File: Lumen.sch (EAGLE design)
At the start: 33 parts, among them J1 AVR_SPI_PRG_6PTH, U1 Tiny45-20-SMT, Y1 8Mhz

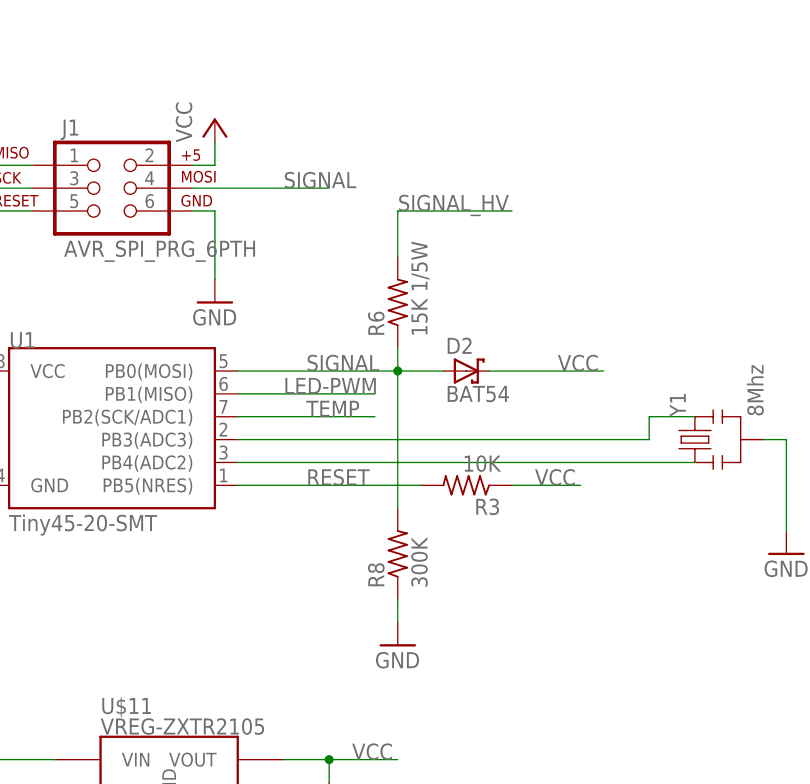
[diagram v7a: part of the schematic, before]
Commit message: Rearranged boards for manufacturability. Changed 0402 footprint.
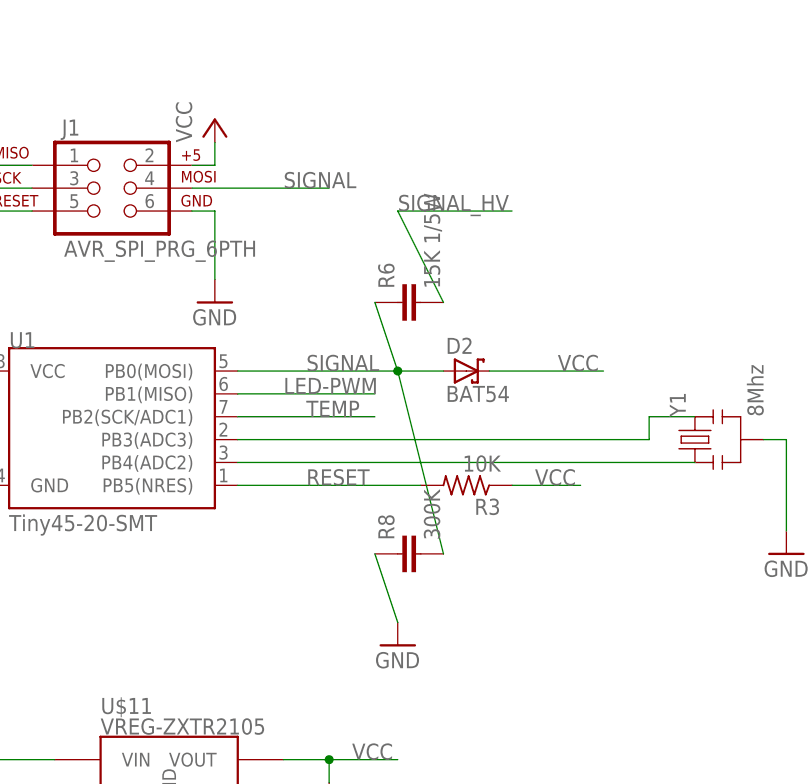
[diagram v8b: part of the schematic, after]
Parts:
- R6, R8: device resistor:R-US_R0402 -> BlueRobotics-Main:C-EUC0402
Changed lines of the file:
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@@
 <part name="R7" library="resistor" deviceset="R-US_" device="R1206" value="NP"/>
 <part name="GND15" library="supply1" deviceset="GND" device=""/>
-<part name="R6" library="resistor" deviceset="R-US_" device="R0402" value="15K 1/5W"/>
-<part name="R8" library="resistor" deviceset="R-US_" device="R0402" value="300K"/>
+<part name="R6" library="BlueRobotics-Main" deviceset="C-EU" device="C0402" value="15K 1/5W"/>
+<part name="R8" library="BlueRobotics-Main" deviceset="C-EU" device="C0402" value="300K"/>
 <part name="Y1" library="SparkFun" deviceset="RESONATOR" device="SMD" value="8Mhz"/>
 </parts>
@@
 <segment>
 <pinref part="GND15" gate="1" pin="GND"/>
-<wire x1="88.9" y1="45.72" x2="88.9" y2="48.26" width="0.1524" layer="91"/>
+<wire x1="88.9" y1="45.72" x2="86.36" y2="53.34" width="0.1524" layer="91"/>
 <pinref part="R8" gate="G$1" pin="1"/>
 </segment>
@@
 <pinref part="D2" gate="G$1" pin="A"/>
 <wire x1="88.9" y1="73.66" x2="93.98" y2="73.66" width="0.1524" layer="91"/>
-<wire x1="88.9" y1="76.2" x2="88.9" y2="73.66" width="0.1524" layer="91"/>
+<wire x1="86.36" y1="81.28" x2="88.9" y2="73.66" width="0.1524" layer="91"/>
 <junction x="88.9" y="73.66"/>
-<wire x1="88.9" y1="58.42" x2="88.9" y2="73.66" width="0.1524" layer="91"/>
+<wire x1="93.98" y1="53.34" x2="88.9" y2="73.66" width="0.1524" layer="91"/>
 <pinref part="R6" gate="G$1" pin="1"/>
 <pinref part="R8" gate="G$1" pin="2"/>
@@
 <net name="SIGNAL_HV" class="0">
 <segment>
-<wire x1="88.9" y1="86.36" x2="88.9" y2="91.44" width="0.1524" layer="91"/>
+<wire x1="93.98" y1="81.28" x2="88.9" y2="91.44" width="0.1524" layer="91"/>
 <wire x1="88.9" y1="91.44" x2="101.6" y2="91.44" width="0.1524" layer="91"/>
 <label x="88.9" y="91.44" size="1.778" layer="95"/>
